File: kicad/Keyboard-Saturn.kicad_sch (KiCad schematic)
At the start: 215 parts, among them J1 OLED_128x32, SW0 SW_Push, SW1 SW_Push, SW10 SW_Push, SW100 SW_Push, SW101 SW_Push, SW102 SW_Push, SW103 SW_Push, SW104 SW_Push, SW11 SW_Push, SW12 SW_Push, SW13 SW_Push, SW14 SW_Push, SW15 SW_Push, SW16 SW_Push, SW17 SW_Push, SW18 SW_Push, SW19 SW_Push, SW2 SW_Push, SW20 SW_Push, SW21 SW_Push, SW22 SW_Push, SW23 SW_Push, SW24 SW_Push, SW25 SW_Push, SW26 SW_Push, SW27 SW_Push, SW28 SW_Push, SW29 SW_Push, SW30 SW_Push, SW31 SW_Push, SW32 SW_Push, SW33 SW_Push, SW34 SW_Push, SW35 SW_Push, SW36 SW_Push, SW37 SW_Push, SW38 SW_Push, SW39 SW_Push, SW4 SW_Push, SW40 SW_Push, SW41 SW_Push, SW42 SW_Push, SW43 SW_Push, SW44 SW_Push, SW45 SW_Push, SW46 SW_Push, SW47 SW_Push, SW48 SW_Push, SW49 SW_Push, SW5 SW_Push, SW50 SW_Push, SW51 SW_Push, SW52 SW_Push, SW53 SW_Push, SW54 SW_Push, SW55 SW_Push, SW56 SW_Push, SW57 SW_Push, SW58 SW_Push, SW59 SW_Push, SW6 SW_Push, SW60 SW_Push, SW61 SW_Push, SW62 SW_Push, SW63 SW_Push, SW64 SW_Push, SW65 SW_Push, SW66 SW_Push, SW67 SW_Push, SW68 SW_Push, SW69 SW_Push, SW7 SW_Push, SW70 SW_Push, SW71 SW_Push, SW72 SW_Push, SW73 SW_Push, SW74 SW_Push, SW75 SW_Push, SW76 SW_Push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

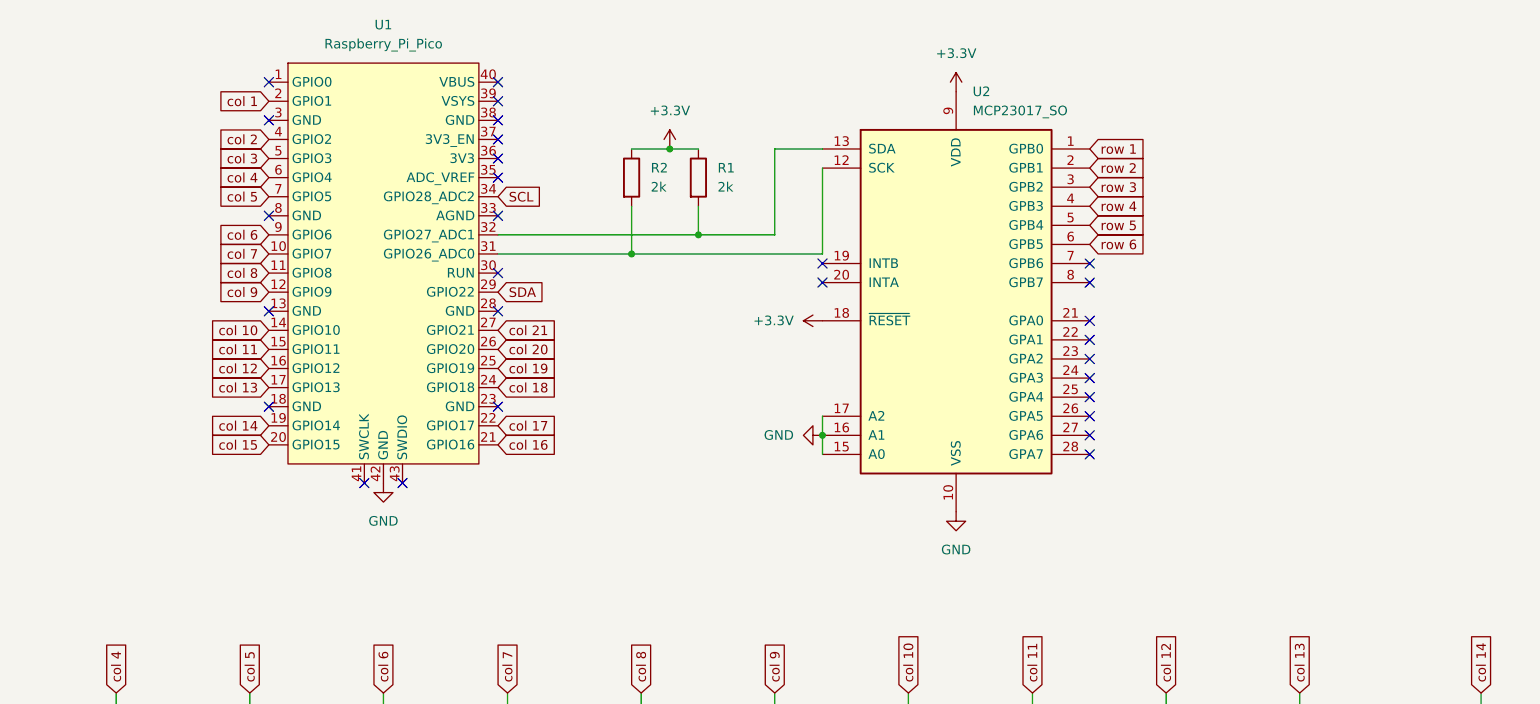
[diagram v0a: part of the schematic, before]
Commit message: added SN34HC165N to kicad
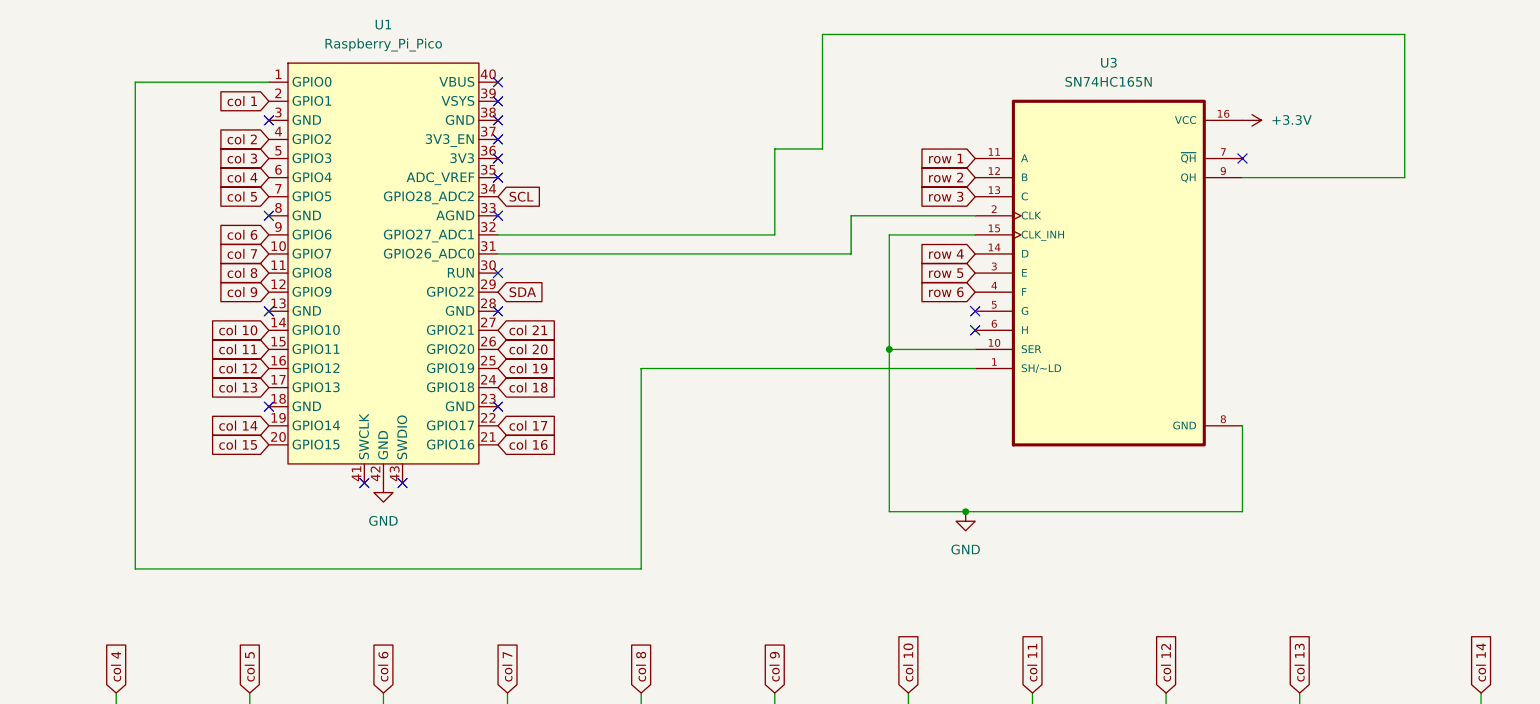
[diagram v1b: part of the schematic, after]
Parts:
- removed R1, R2: 2k, Resistor_THT:R_Axial_DIN0204_L3.6mm_D1.6mm_P7.62mm_Horizontal, symbol Device:R
- removed U2: MCP23017_SO, Package_SO:SOIC-28W_7.5x17.9mm_P1.27mm, symbol Interface_Expansion:MCP23017_SO
- added U3: SN74HC165N, Keyboard-Saturn:DIP794W45P254L1969H508Q16, symbol SN74HC165N:SN74HC165N
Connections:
- net +3.3V: now also U3.16 (VCC)
- net GND: now also U3.10 (SER), U3.15 (CLK_INH), U3.8 (GND)
- net row 1: now also U3.11 (A)
- net row 2: now also U3.12 (B)
- net row 3: now also U3.13 (C)
- net row 4: now also U3.14 (D)
- net row 5: now also U3.3 (E)
- net row 6: now also U3.4 (F)
- net at U1.32 (GPIO27_ADC1): now also U3.9 (QH)
- net at U1.31 (GPIO26_ADC0): now also U3.2 (CLK)
- net at U1.1 (GPIO0): now also U3.1 (SH/~LD)
- no-connect marks 29 -> 19

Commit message: 90% done firmware, updated kicad files to match code
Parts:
- SW1: value SW_Push -> KC_ESCAPE
- SW10: value SW_Push -> KC_F9
- SW100: value SW_Push -> KC_KP_MINUS
- SW101: value SW_Push -> KC_KP_1
- SW102: value SW_Push -> KC_KP_PLUS
- SW103: value SW_Push -> KC_KP_2
- SW104: value SW_Push -> KC_KP_3
- SW11: value SW_Push -> KC_F10
- SW12: value SW_Push -> KC_F11
- SW13: value SW_Push -> KC_F12
- SW14: value SW_Push -> KC_GRAVE
- SW15: value SW_Push -> KC_1
- SW16: value SW_Push -> KC_2
- SW17: value SW_Push -> KC_3
- SW18: value SW_Push -> KC_4
- SW19: value SW_Push -> KC_5
- SW2: value SW_Push -> KC_F1
- SW20: value SW_Push -> KC_6
- SW21: value SW_Push -> KC_7
- SW22: value SW_Push -> KC_8
- SW23: value SW_Push -> KC_9
- SW24: value SW_Push -> KC_0
- SW25: value SW_Push -> KC_MINUS
- SW26: value SW_Push -> KC_EQUAL
- SW27: value SW_Push -> KC_BACKSPACE
- SW28: value SW_Push -> KC_TAB
- SW29: value SW_Push -> KC_Q
- SW3: renamed from F2; value SW_Push -> KC_F2
- SW30: value SW_Push -> KC_W
- SW31: value SW_Push -> KC_E
- SW32: value SW_Push -> KC_R
- SW33: value SW_Push -> KC_T
- SW34: value SW_Push -> KC_Y
- SW35: value SW_Push -> KC_U
- SW36: value SW_Push -> KC_I
- SW37: value SW_Push -> KC_O
- SW38: value SW_Push -> KC_P
- SW39: value SW_Push -> KC_LEFT_BRACKET
- SW4: value SW_Push -> KC_F3
- SW40: value SW_Push -> KC_RIGHT_BRACKET
- SW41: value SW_Push -> KC_BACKSLASH
- SW42: value SW_Push -> KC_CAPS_LOCK
- SW43: value SW_Push -> KC_A
- SW44: value SW_Push -> KC_S
- SW45: value SW_Push -> KC_D
- SW46: value SW_Push -> KC_F
- SW47: value SW_Push -> KC_G
- SW48: value SW_Push -> KC_H
- SW49: value SW_Push -> KC_J
- SW5: value SW_Push -> KC_F4
- SW50: value SW_Push -> KC_K
- SW51: value SW_Push -> KC_L
- SW52: value SW_Push -> KC_SEMICOLON
- SW53: value SW_Push -> KC_QUOTE
- SW54: value SW_Push -> KC_ENTER
- SW55: value SW_Push -> KC_LEFT_SHIFT
- SW56: value SW_Push -> KC_Z
- SW57: value SW_Push -> KC_X
- SW58: value SW_Push -> KC_C
- SW59: value SW_Push -> KC_V
- SW6: value SW_Push -> KC_F5
- SW60: value SW_Push -> KC_B
- SW61: value SW_Push -> KC_N
- SW62: value SW_Push -> KC_M
- SW63: value SW_Push -> KC_COMMA
- SW64: value SW_Push -> KC_DOT
- SW65: value SW_Push -> KC_SLASH
- SW66: value SW_Push -> KC_RIGHT_SHIFT
- SW67: value SW_Push -> KC_LEFT_CTRL
- SW68: value SW_Push -> KC_LEFT_GUI
- SW69: value SW_Push -> KC_LEFT_ALT
- SW7: value SW_Push -> KC_F6
- SW70: value SW_Push -> KC_SPACE
- SW71: value SW_Push -> KC_RIGHT_ALT
- SW72: value SW_Push -> KC_APPLICATION
- SW73: value SW_Push -> KC_RIGHT_GUI
- SW74: value SW_Push -> KC_RIGHT_CTRL
- SW75: value SW_Push -> KC_PRINT_SCREEN
- SW76: value SW_Push -> KC_INSERT
- SW77: value SW_Push -> KC_DELETE
- SW78: value SW_Push -> KC_SCROLL_LOCK
- SW79: value SW_Push -> KC_HOME
- SW8: value SW_Push -> KC_F7
- SW80: renamed from SW0; value SW_Push -> KC_END
- SW81: value SW_Push -> KC_PAUSE
- SW82: value SW_Push -> KC_PAGE_UP
- SW83: value SW_Push -> KC_PAGE_DOWN
- SW84: value SW_Push -> KC_NUM_LOCK
- SW85: value SW_Push -> KC_LEFT
- SW86: value SW_Push -> KC_UP
- SW87: value SW_Push -> KC_DOWN
- SW88: value SW_Push -> KC_KP_7
- SW89: value SW_Push -> KC_RIGHT
- SW9: value SW_Push -> KC_F8
- SW90: value SW_Push -> KC_KP_4
- SW91: value SW_Push -> KC_KP_0
- SW92: value SW_Push -> KC_KP_SLASH
- SW93: value SW_Push -> KC_KP_8
- SW94: value SW_Push -> KC_KP_5
- SW95: value SW_Push -> KC_KP_ENTER
- SW96: value SW_Push -> KC_KP_ASTERISK
- SW97: value SW_Push -> KC_KP_9
- SW98: value SW_Push -> KC_KP_6
- SW99: value SW_Push -> KC_KP_DOT
